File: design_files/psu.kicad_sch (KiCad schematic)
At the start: 13 parts, among them U7 PUMH10,115, U8 LMR51430

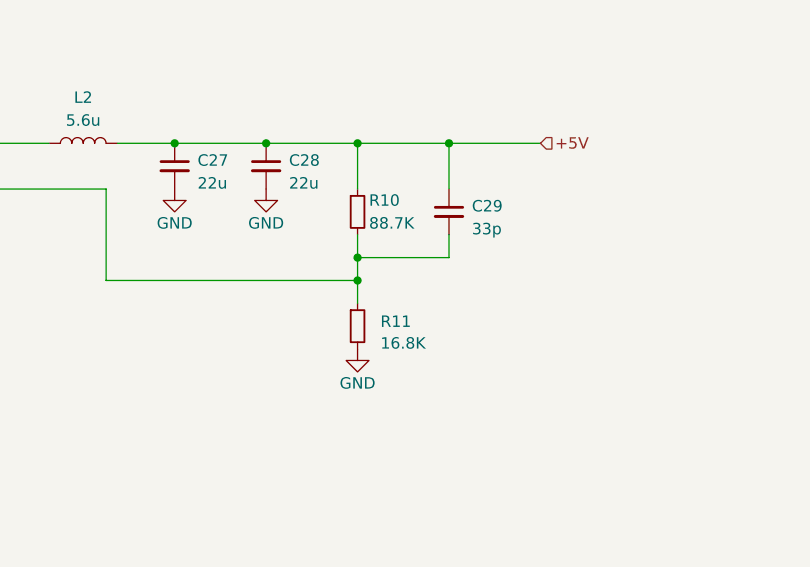
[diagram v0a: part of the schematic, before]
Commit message: Changed values in schematic
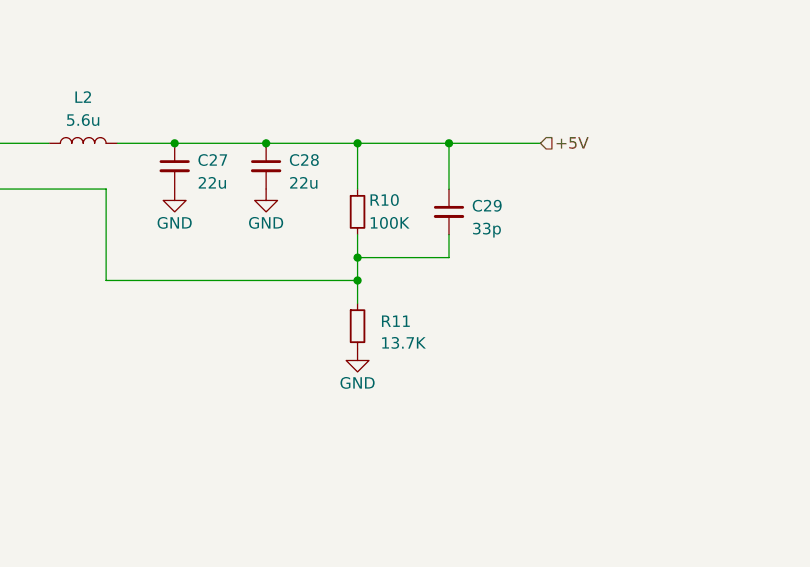
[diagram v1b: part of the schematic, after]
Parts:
- R10: value 88.7K -> 100K
- R11: value 16.8K -> 13.7K
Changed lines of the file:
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@@
 			)
 		)
-		(property "Value" "16.8K"
+		(property "Value" "13.7K"
 			(at 200.66 73.0249 0)
 			(effects
@@
 			)
 		)
-		(property "Value" "88.7K"
+		(property "Value" "100K"
 			(at 199.39 59.69 0)
 			(effects
